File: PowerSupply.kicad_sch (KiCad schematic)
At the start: 8 parts, among them U501 TPSM33625

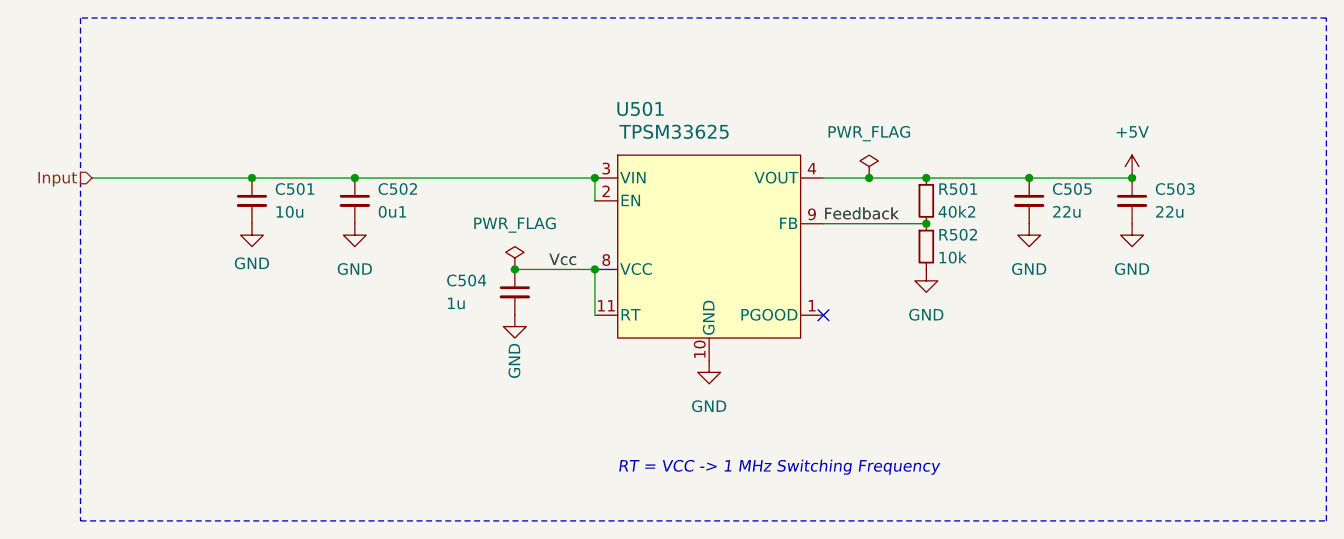
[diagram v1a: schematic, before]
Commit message: Update DCDC
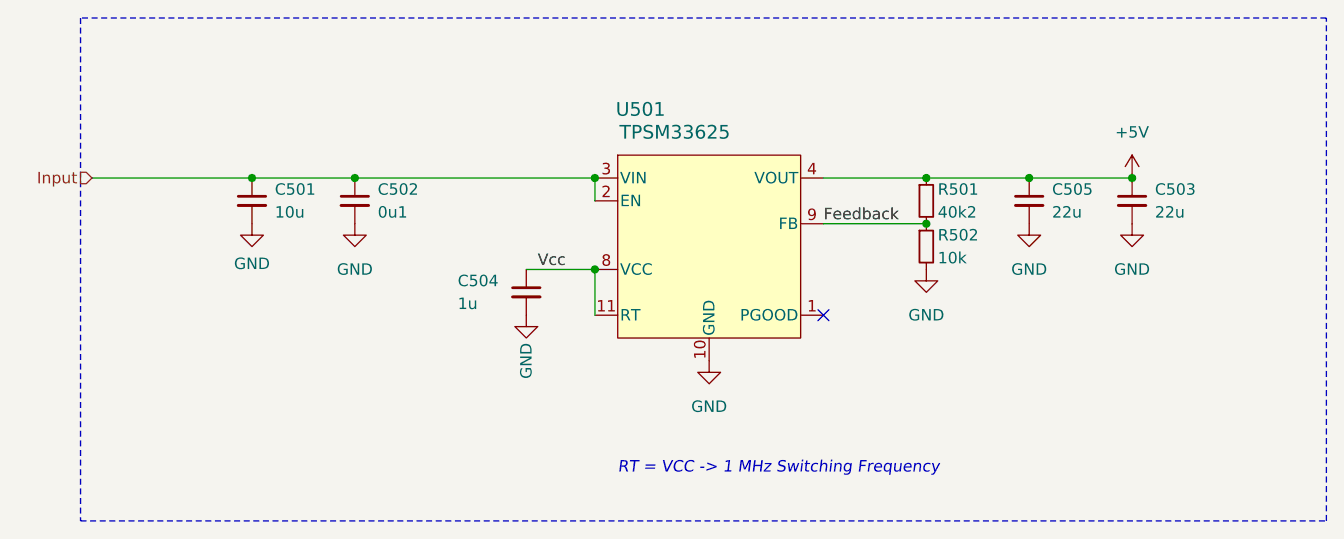
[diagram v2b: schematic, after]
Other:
- moved on the sheet: C504
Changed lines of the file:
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@@
 	(title_block
 		(title "Power Supply")
-		(date "2023-08-08")
-		(rev "2")
+		(date "2024-03-28")
+		(rev "3")
 		(company "+5V")
 	)
@@
 	)
 	(junction
-		(at 176.53 96.52)
-		(diameter 0)
-		(color 0 0 0 0)
-	)
-	(junction
-		(at 137.16 106.68)
-		(diameter 0)
-		(color 0 0 0 0)
-	)
-	(junction
 		(at 182.88 96.52)
 		(diameter 0)
@@
 	(wire
 		(pts
-			(xy 137.16 106.68) (xy 146.05 106.68)
+			(xy 138.43 106.68) (xy 146.05 106.68)
 		)
 		(stroke
@@
 	(wire
 		(pts
-			(xy 176.53 96.52) (xy 182.88 96.52)
+			(xy 107.95 96.52) (xy 119.38 96.52)
 		)
 		(stroke
@@
 	(wire
 		(pts
-			(xy 107.95 96.52) (xy 119.38 96.52)
+			(xy 171.45 101.6) (xy 182.88 101.6)
 		)
 		(stroke
@@
 	(wire
 		(pts
-			(xy 171.45 101.6) (xy 182.88 101.6)
+			(xy 194.31 96.52) (xy 205.74 96.52)
 		)
 		(stroke
@@
 	(wire
 		(pts
-			(xy 194.31 96.52) (xy 205.74 96.52)
-		)
-		(stroke
-			(width 0)
-			(type default)
-		)
-	)
-	(wire
-		(pts
-			(xy 171.45 96.52) (xy 176.53 96.52)
+			(xy 171.45 96.52) (xy 182.88 96.52)
 		)
 		(stroke
@@
 	)
 	(label "Vcc"
-		(at 140.97 106.68 0)
+		(at 139.7 106.68 0)
 		(fields_autoplaced yes)
 		(effects
@@
 					(unit 1)
 				)
+				(path "/6c8448b4-b04d-47e1-934e-e40cbe27a7be"
+					(reference "#PWR0508")
+					(unit 1)
+				)
 			)
 		)
@@
 	(symbol
 		(lib_id "power:GND")
-		(at 137.16 111.76 0)
+		(at 138.43 111.76 0)
 		(unit 1)
 		(exclude_from_sim no)
@@
 		(dnp no)
 		(property "Reference" "#PWR0506"
-			(at 137.16 118.11 0)
+			(at 138.43 118.11 0)
 			(effects
 				(font
@@
 		)
 		(property "Value" "GND"
-			(at 137.16 116.84 90)
+			(at 138.43 116.84 90)
 			(effects
 				(font
@@
 		)
 		(property "Footprint" ""
-			(at 137.16 111.76 0)
+			(at 138.43 111.76 0)
 			(effects
 				(font
@@
 		)
 		(property "Datasheet" ""
-			(at 137.16 111.76 0)
-			(effects
-				(font
-					(size 1.27 1.27)
-				)
-				(hide yes)
-			)
-		)
-		(property "Description" ""
-			(at 137.16 111.76 0)
-			(effects
-				(font
-					(size 1.27 1.27)
-				)
-				(hide yes)
-			)
-		)
-		(pin "1"
-		)
-		(instances
-			(project "control"
-				(path "/6c8448b4-b04d-47e1-934e-e40cbe27a7be/24a9dc0c-cb3c-464a-a734-f09bf949d71a"
+			(at 138.43 111.76 0)
+			(effects
+				(font
+					(size 1.27 1.27)
+				)
+				(hide yes)
+			)
+		)
+		(property "Description" ""
+			(at 138.43 111.76 0)
+			(effects
+				(font
+					(size 1.27 1.27)
+				)
+				(hide yes)
+			)
+		)
+		(pin "1"
+		)
+		(instances
+			(project "control"
+				(path "/6c8448b4-b04d-47e1-934e-e40cbe27a7be/24a9dc0c-cb3c-464a-a734-f09bf949d71a"
+					(reference "#PWR0506")
+					(unit 1)
+				)
+				(path "/6c8448b4-b04d-47e1-934e-e40cbe27a7be"
 					(reference "#PWR0506")
 					(unit 1)
@@
 					(unit 1)
 				)
+				(path "/6c8448b4-b04d-47e1-934e-e40cbe27a7be"
+					(reference "R502")
+					(unit 1)
+				)
 			)
 		)
@@
 					(unit 1)
 				)
+				(path "/6c8448b4-b04d-47e1-934e-e40cbe27a7be"
+					(reference "U501")
+					(unit 1)
+				)
 			)
 		)
@@
 					(unit 1)
 				)
+				(path "/6c8448b4-b04d-47e1-934e-e40cbe27a7be"
+					(reference "R501")
+					(unit 1)
+				)
 			)
 		)
@@
 					(unit 1)
 				)
+				(path "/6c8448b4-b04d-47e1-934e-e40cbe27a7be"
+					(reference "#PWR0505")
+					(unit 1)
+				)
 			)
 		)
@@
 					(unit 1)
 				)
+				(path "/6c8448b4-b04d-47e1-934e-e40cbe27a7be"
+					(reference "#PWR0503")
+					(unit 1)
+				)
 			)
 		)
@@
 					(unit 1)
 				)
+				(path "/6c8448b4-b04d-47e1-934e-e40cbe27a7be"
+					(reference "C501")
+					(unit 1)
+				)
 			)
 		)
@@
 	(symbol
 		(lib_id "Device:C_Small")
-		(at 137.16 109.22 0)
+		(at 138.43 109.22 0)
 		(unit 1)
 		(exclude_from_sim no)
@@
 		(dnp no)
 		(property "Reference" "C504"
-			(at 129.54 107.95 0)
+			(at 130.81 107.95 0)
 			(effects
 				(font
@@
 		)
 		(property "Value" "1u"
-			(at 129.54 110.49 0)
+			(at 130.81 110.49 0)
 			(effects
 				(font
@@
 		)
 		(property "Footprint" "Capacitor_SMD:C_0603_1608Metric"
-			(at 137.16 109.22 0)
+			(at 138.43 109.22 0)
 			(effects
 				(font
@@
 		)
 		(property "Datasheet" "~"
-			(at 137.16 109.22 0)
-			(effects
-				(font
-					(size 1.27 1.27)
-				)
-				(hide yes)
-			)
-		)
-		(property "Description" ""
-			(at 137.16 109.22 0)
+			(at 138.43 109.22 0)
+			(effects
+				(font
+					(size 1.27 1.27)
+				)
+				(hide yes)
+			)
+		)
+		(property "Description" ""
+			(at 138.43 109.22 0)
 			(effects
 				(font
@@
 			(project "control"
 				(path "/6c8448b4-b04d-47e1-934e-e40cbe27a7be/24a9dc0c-cb3c-464a-a734-f09bf949d71a"
+					(reference "C504")
+					(unit 1)
+				)
+				(path "/6c8448b4-b04d-47e1-934e-e40cbe27a7be"
 					(reference "C504")
 					(unit 1)
@@
 					(unit 1)
 				)
-			)
-		)
-	)
-	(symbol
-		(lib_id "power:PWR_FLAG")
-		(at 137.16 106.68 0)
-		(unit 1)
-		(exclude_from_sim no)
-		(in_bom yes)
-		(on_board yes)
-		(dnp no)
-		(fields_autoplaced yes)
-		(property "Reference" "#FLG0502"
-			(at 137.16 104.775 0)
-			(effects
-				(font
-					(size 1.27 1.27)
-				)
-				(hide yes)
-			)
-		)
-		(property "Value" "PWR_FLAG"
-			(at 137.16 101.6 0)
-			(effects
-				(font
-					(size 1.27 1.27)
-				)
-			)
-		)
-		(property "Footprint" ""
-			(at 137.16 106.68 0)
-			(effects
-				(font
-					(size 1.27 1.27)
-				)
-				(hide yes)
-			)
-		)
-		(property "Datasheet" "~"
-			(at 137.16 106.68 0)
-			(effects
-				(font
-					(size 1.27 1.27)
-				)
-				(hide yes)
-			)
-		)
-		(property "Description" ""
-			(at 137.16 106.68 0)
-			(effects
-				(font
-					(size 1.27 1.27)
-				)
-				(hide yes)
-			)
-		)
-		(pin "1"
-		)
-		(instances
-			(project "control"
-				(path "/6c8448b4-b04d-47e1-934e-e40cbe27a7be/24a9dc0c-cb3c-464a-a734-f09bf949d71a"
-					(reference "#FLG0502")
+				(path "/6c8448b4-b04d-47e1-934e-e40cbe27a7be"
+					(reference "C505")
 					(unit 1)
 				)
@@
 					(unit 1)
 				)
+				(path "/6c8448b4-b04d-47e1-934e-e40cbe27a7be"
+					(reference "C502")
+					(unit 1)
+				)
 			)
 		)
@@
 					(unit 1)
 				)
+				(path "/6c8448b4-b04d-47e1-934e-e40cbe27a7be"
+					(reference "#PWR0502")
+					(unit 1)
+				)
 			)
 		)
@@
 					(unit 1)
 				)
-			)
-		)
-	)
-	(symbol
-		(lib_id "power:PWR_FLAG")
-		(at 176.53 96.52 0)
-		(unit 1)
-		(exclude_from_sim no)
-		(in_bom yes)
-		(on_board yes)
-		(dnp no)
-		(fields_autoplaced yes)
-		(property "Reference" "#FLG0501"
-			(at 176.53 94.615 0)
-			(effects
-				(font
-					(size 1.27 1.27)
-				)
-				(hide yes)
-			)
-		)
-		(property "Value" "PWR_FLAG"
-			(at 176.53 91.44 0)
-			(effects
-				(font
-					(size 1.27 1.27)
-				)
-			)
-		)
-		(property "Footprint" ""
-			(at 176.53 96.52 0)
-			(effects
-				(font
-					(size 1.27 1.27)
-				)
-				(hide yes)
-			)
-		)
-		(property "Datasheet" "~"
-			(at 176.53 96.52 0)
-			(effects
-				(font
-					(size 1.27 1.27)
-				)
-				(hide yes)
-			)
-		)
-		(property "Description" ""
-			(at 176.53 96.52 0)
-			(effects
-				(font
-					(size 1.27 1.27)
-				)
-				(hide yes)
-			)
-		)
-		(pin "1"
-		)
-		(instances
-			(project "control"
-				(path "/6c8448b4-b04d-47e1-934e-e40cbe27a7be/24a9dc0c-cb3c-464a-a734-f09bf949d71a"
-					(reference "#FLG0501")
+				(path "/6c8448b4-b04d-47e1-934e-e40cbe27a7be"
+					(reference "#PWR0504")
 					(unit 1)
 				)
@@
 					(unit 1)
 				)
+				(path "/6c8448b4-b04d-47e1-934e-e40cbe27a7be"
+					(reference "#PWR0501")
+					(unit 1)
+				)
 			)
 		)
@@
 					(unit 1)
 				)
+				(path "/6c8448b4-b04d-47e1-934e-e40cbe27a7be"
+					(reference "#PWR0507")
+					(unit 1)
+				)
 			)
 		)
@@
 					(reference "C503")
 					(unit 1)
+				)
+				(path "/6c8448b4-b04d-47e1-934e-e40cbe27a7be"
+					(reference "C503")
+					(unit 1)

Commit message: Refresh
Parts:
- renumbered C505 to C503, C503 to C504, C504 to C505
